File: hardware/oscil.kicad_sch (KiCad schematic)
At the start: 0 parts

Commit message: Add sheet hierarchy and build log
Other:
- added sheet 01_power (01_power.kicad_sch)
- added sheet 02_afe_ch1 (02_afe_ch1.kicad_sch)
- added sheet 03_afe_ch2 (03_afe_ch2.kicad_sch)
- added sheet 04_acq (04_acq.kicad_sch)
- added sheet 05_display (05_display.kicad_sch)
- added sheet 06_gen (06_gen.kicad_sch)
- title: (none) -> Oscil

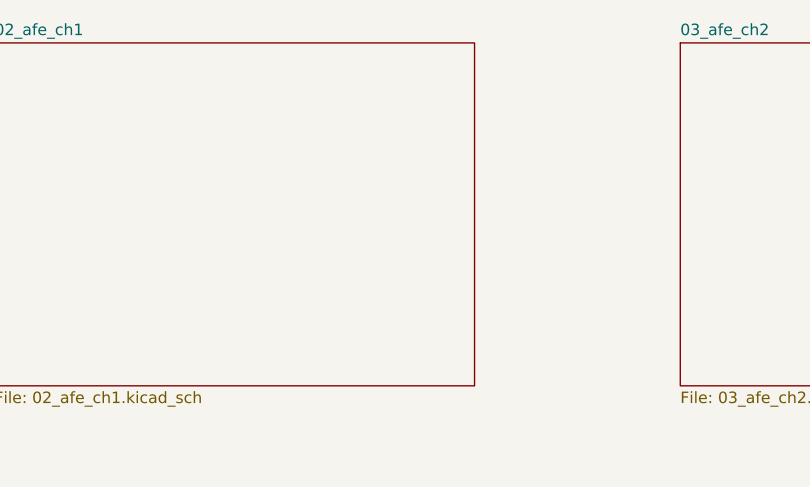
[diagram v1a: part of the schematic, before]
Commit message: AFE channel 1: divider, compensation, clamp, buffer, filter
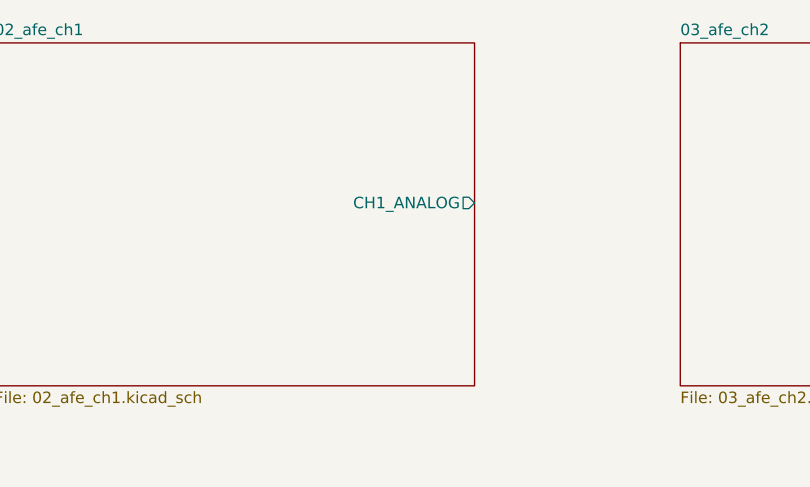
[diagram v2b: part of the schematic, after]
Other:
- sheet 02_afe_ch1 ports: added CH1_ANALOG; removed none
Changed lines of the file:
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@@
+			)
+		)
+		(pin "CH1_ANALOG" output
+			(at 217.17 87.63 0)
+			(effects
+				(font
+					(size 1.27 1.27)
+				)
+				(justify right)
 			)
 		)

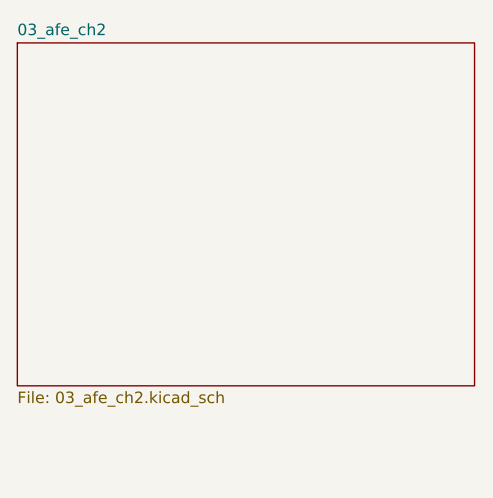
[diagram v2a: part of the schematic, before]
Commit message: AFE channel 2: copy of channel 1
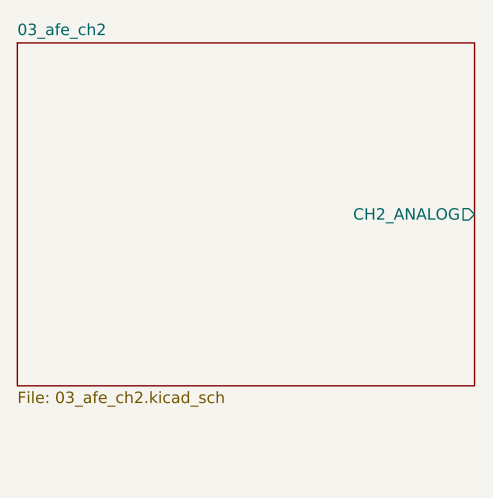
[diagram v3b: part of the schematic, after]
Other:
- sheet 03_afe_ch2 ports: added CH2_ANALOG; removed none
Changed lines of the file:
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@@
+			)
+		)
+		(pin "CH2_ANALOG" output
+			(at 290.83 88.9 0)
+			(effects
+				(font
+					(size 1.27 1.27)
+				)
+				(justify right)
 			)
 		)

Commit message: Acquisition sheet: ADC pair, module, front panel
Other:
- sheet 04_acq ports: added CH1_ANALOG, CH2_ANALOG, LINK1_RX, LINK1_TX; removed none
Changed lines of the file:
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@@
 		(comment 2 "ESP32-S3 / ESP-IDF / FreeRTOS")
+	)
+	(wire
+		(pts
+			(xy 90.17 118.11) (xy 90.17 152.4)
+		)
+		(stroke
+			(width 0)
+			(type default)
+		)
+	)
+	(wire
+		(pts
+			(xy 294.64 88.9) (xy 290.83 88.9)
+		)
+		(stroke
+			(width 0)
+			(type default)
+		)
+	)
+	(wire
+		(pts
+			(xy 220.98 87.63) (xy 220.98 118.11)
+		)
+		(stroke
+			(width 0)
+			(type default)
+		)
+	)
+	(wire
+		(pts
+			(xy 217.17 87.63) (xy 220.98 87.63)
+		)
+		(stroke
+			(width 0)
+			(type default)
+		)
+	)
+	(wire
+		(pts
+			(xy 294.64 120.65) (xy 294.64 88.9)
+		)
+		(stroke
+			(width 0)
+			(type default)
+		)
+	)
+	(wire
+		(pts
+			(xy 90.17 152.4) (xy 93.98 152.4)
+		)
+		(stroke
+			(width 0)
+			(type default)
+		)
+	)
+	(wire
+		(pts
+			(xy 93.98 160.02) (xy 86.36 160.02)
+		)
+		(stroke
+			(width 0)
+			(type default)
+		)
+	)
+	(wire
+		(pts
+			(xy 86.36 160.02) (xy 86.36 120.65)
+		)
+		(stroke
+			(width 0)
+			(type default)
+		)
+	)
+	(wire
+		(pts
+			(xy 220.98 118.11) (xy 90.17 118.11)
+		)
+		(stroke
+			(width 0)
+			(type default)
+		)
+	)
+	(wire
+		(pts
+			(xy 86.36 120.65) (xy 294.64 120.65)
+		)
+		(stroke
+			(width 0)
+			(type default)
+		)
 	)
 	(sheet
@@
 			)
 		)
+		(pin "CH1_ANALOG" output
+			(at 93.98 152.4 180)
+			(effects
+				(font
+					(size 1.27 1.27)
+				)
+				(justify left)
+			)
+		)
+		(pin "CH2_ANALOG" output
+			(at 93.98 160.02 180)
+			(effects
+				(font
+					(size 1.27 1.27)
+				)
+				(justify left)
+			)
+		)
+		(pin "LINK1_RX" input
+			(at 144.78 153.67 0)
+			(effects
+				(font
+					(size 1.27 1.27)
+				)
+				(justify right)
+			)
+		)
+		(pin "LINK1_TX" output
+			(at 144.78 160.02 0)
+			(effects
+				(font
+					(size 1.27 1.27)
+				)
+				(justify right)
+			)
+		)

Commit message: Display sheet: panel connector, touch, backlight
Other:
- sheet 05_display ports: added LINK1_RX, LINK1_TX, LINK2_TX; removed none
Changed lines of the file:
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@@
+	(wire
+		(pts
+			(xy 144.78 160.02) (xy 165.1 160.02)
+		)
+		(stroke
+			(width 0)
+			(type default)
+		)
+	)
 	(wire
 		(pts
 			(xy 86.36 160.02) (xy 86.36 120.65)
+		)
+		(stroke
+			(width 0)
+			(type default)
+		)
+	)
+	(wire
+		(pts
+			(xy 144.78 153.67) (xy 165.1 153.67)
 		)
 		(stroke
@@
 			)
 		)
+		(pin "LINK1_RX" input
+			(at 165.1 160.02 180)
+			(effects
+				(font
+					(size 1.27 1.27)
+				)
+				(justify left)
+			)
+		)
+		(pin "LINK1_TX" output
+			(at 165.1 153.67 180)
+			(effects
+				(font
+					(size 1.27 1.27)
+				)
+				(justify left)
+			)
+		)
+		(pin "LINK2_TX" output
+			(at 218.44 153.67 0)
+			(effects
+				(font
+					(size 1.27 1.27)
+				)
+				(justify right)
+			)
+		)

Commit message: Generator sheet: R-2R ladder and output stage
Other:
- sheet 06_gen ports: added LINK2_RX; removed none
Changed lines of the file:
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@@
+	(wire
+		(pts
+			(xy 218.44 153.67) (xy 238.76 153.67)
+		)
+		(stroke
+			(width 0)
+			(type default)
+		)
+	)
 	(wire
 		(pts
@@
 			)
 		)
+		(pin "LINK2_RX" input
+			(at 238.76 153.67 180)
+			(effects
+				(font
+					(size 1.27 1.27)
+				)
+				(justify left)
+			)
+		)

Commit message: Add final Rev A schematic PDF and edited footprints
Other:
- note added: "Footprints assigned for BOM and Rev B. Dev board, LCD connector and GT911 have none: Rev A uses the modules directly on a breadboard."
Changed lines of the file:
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@@
 	(title_block
 		(title "Oscil")
-		(date "2026-09-18")
-		(rev "0.1")
+		(date "2026-09-21")
+		(rev "A")
 		(comment 1 "Two-channel Digital Oscilloscope and Function Generator")
 		(comment 2 "ESP32-S3 / ESP-IDF / FreeRTOS")
 	)
+	(text "Footprints assigned for BOM and Rev B. Dev board, LCD\nconnector and GT911 have none: Rev A uses the modules\ndirectly on a breadboard."
+		(exclude_from_sim no)
+		(at 99.822 196.85 0)
+		(effects
+			(font
+				(size 1.27 1.27)
+			)
+		)
+	)
 	(wire
